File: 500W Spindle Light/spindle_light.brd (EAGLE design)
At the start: 52 x 52 mm, 14 parts

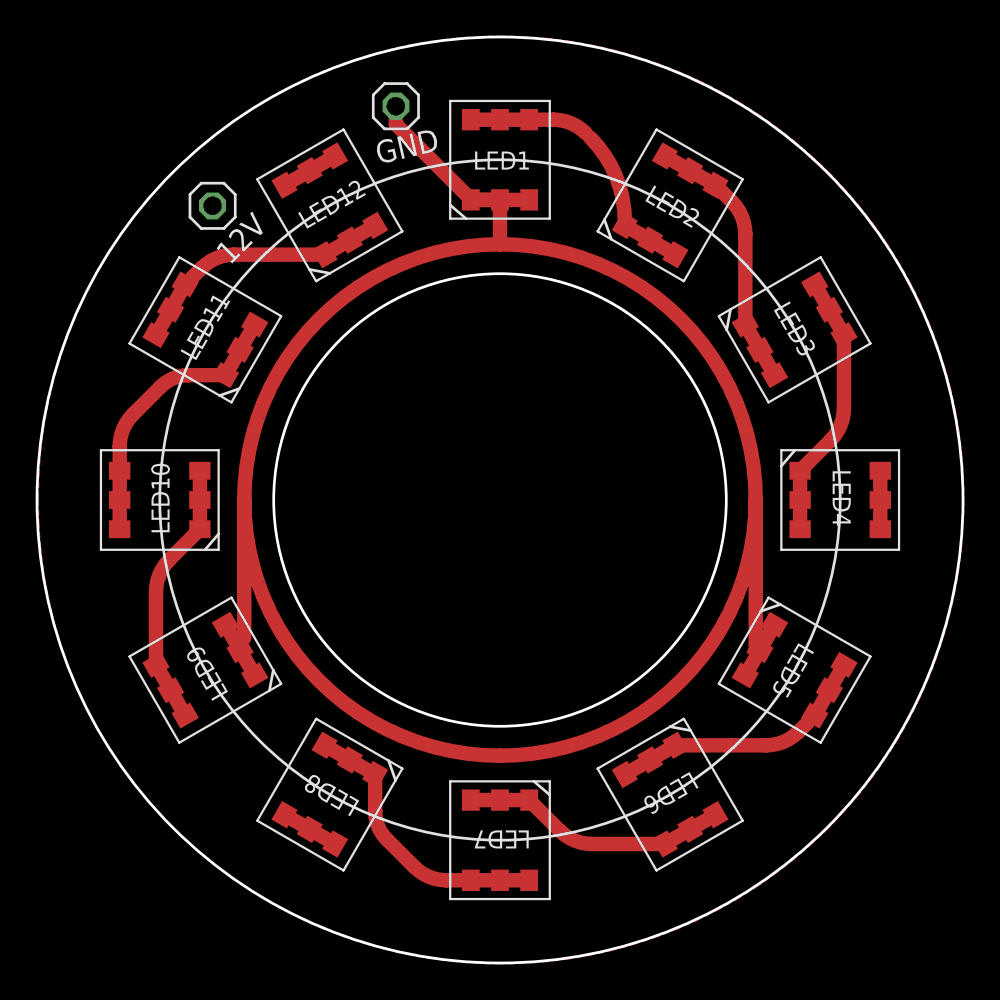
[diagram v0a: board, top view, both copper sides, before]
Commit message: Smaller number of LEDs to make it a bit less bright
Everything connected and prototyped working fine so far. Need to check the dimensions
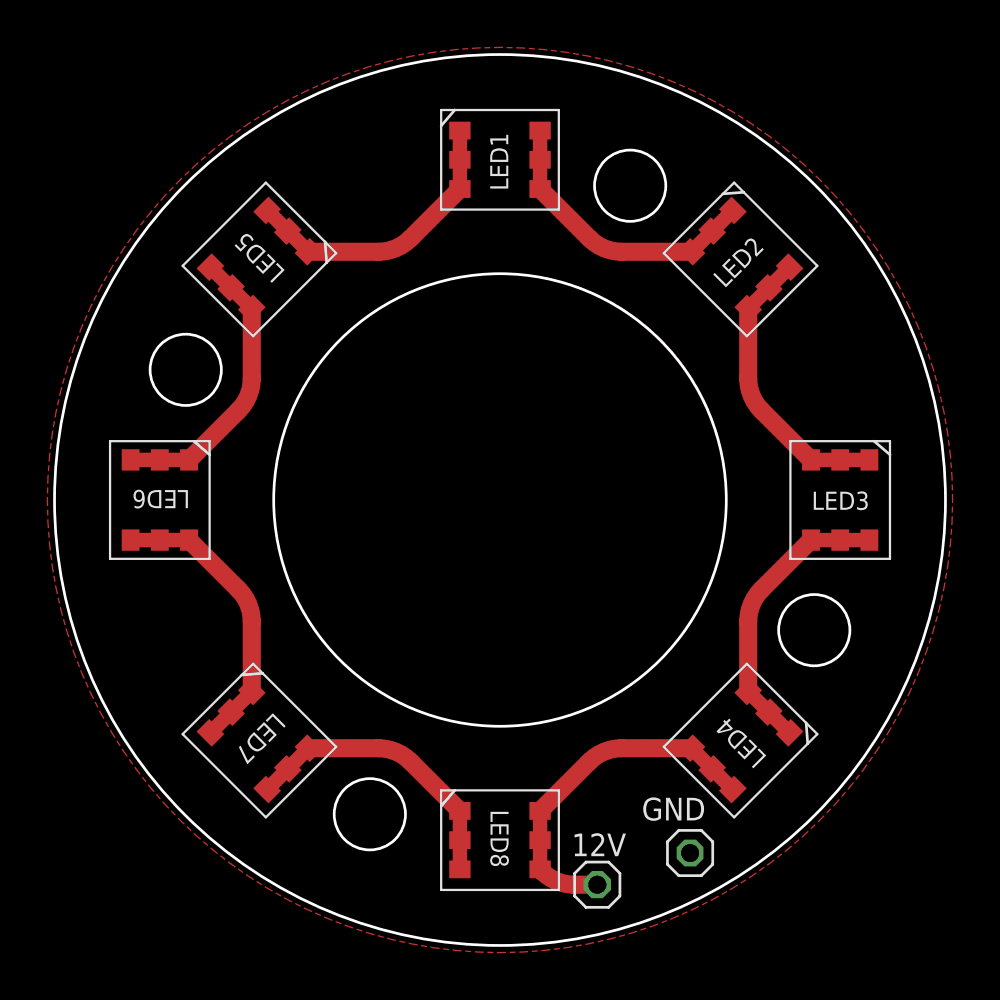
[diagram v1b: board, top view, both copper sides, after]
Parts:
- removed LED10, LED11, LED12, LED9: RF-45HA50DS-EE-Y, NikodemBartnik:5050LED
- moved GND 45.0 mm to (10.7, -19.8)
- moved 12V 43.8 mm to (5.46, -21.6)
- moved LED5 37.9 mm to (-13.5, 13.5), turned to 225 degrees
- moved LED6 33.1 mm to (-19.1, 0.00), turned to 270 degrees
- moved LED4 14.6 mm to (13.5, -13.5), turned to 225 degrees
- moved LED7 14.6 mm to (-13.5, -13.5), turned to 315 degrees
- moved LED3 9.89 mm to (19.1, 0.00), turned to 270 degrees
- moved LED8 9.89 mm to (0.00, -19.1), turned to 0 degrees
- moved LED2 4.98 mm to (13.5, 13.5), turned to 315 degrees
- turned LED1 to 0 degrees
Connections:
- removed net N$1: LED10.P$1, LED10.P$2, LED10.P$3, LED9.P$4, LED9.P$5, LED9.P$6
- removed net N$6: LED10.P$4, LED10.P$5, LED10.P$6, LED11.P$1, LED11.P$2, LED11.P$3
- removed net N$7: LED11.P$4, LED11.P$5, LED11.P$6, LED12.P$1, LED12.P$2, LED12.P$3
- net +12V: no longer LED12.P$4, LED12.P$5, LED12.P$6
- net GND: no longer LED9.P$1, LED9.P$2, LED9.P$3
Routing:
- net GND: track 119.3 -> 16.4 mm
- net N$6: track 15.8 -> 0.00 mm
- net N$1: track 15.0 -> 0.00 mm
- net N$7: track 14.9 -> 0.00 mm
- net +12V: track 9.84 -> 19.8 mm
- net N$4: track 14.9 -> 16.4 mm
- net N$2: track 14.9 -> 16.4 mm
- net N$9: track 15.0 -> 16.4 mm
- net N$5: track 15.0 -> 16.4 mm
- net N$3: track 15.6 -> 16.4 mm
- net N$8: track 15.8 -> 16.4 mm
- added copper zone on layer 1, net GND
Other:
- board size 52 x 52 mm -> 50 x 50 mm
